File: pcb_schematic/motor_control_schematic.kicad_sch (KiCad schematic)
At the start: 1 part

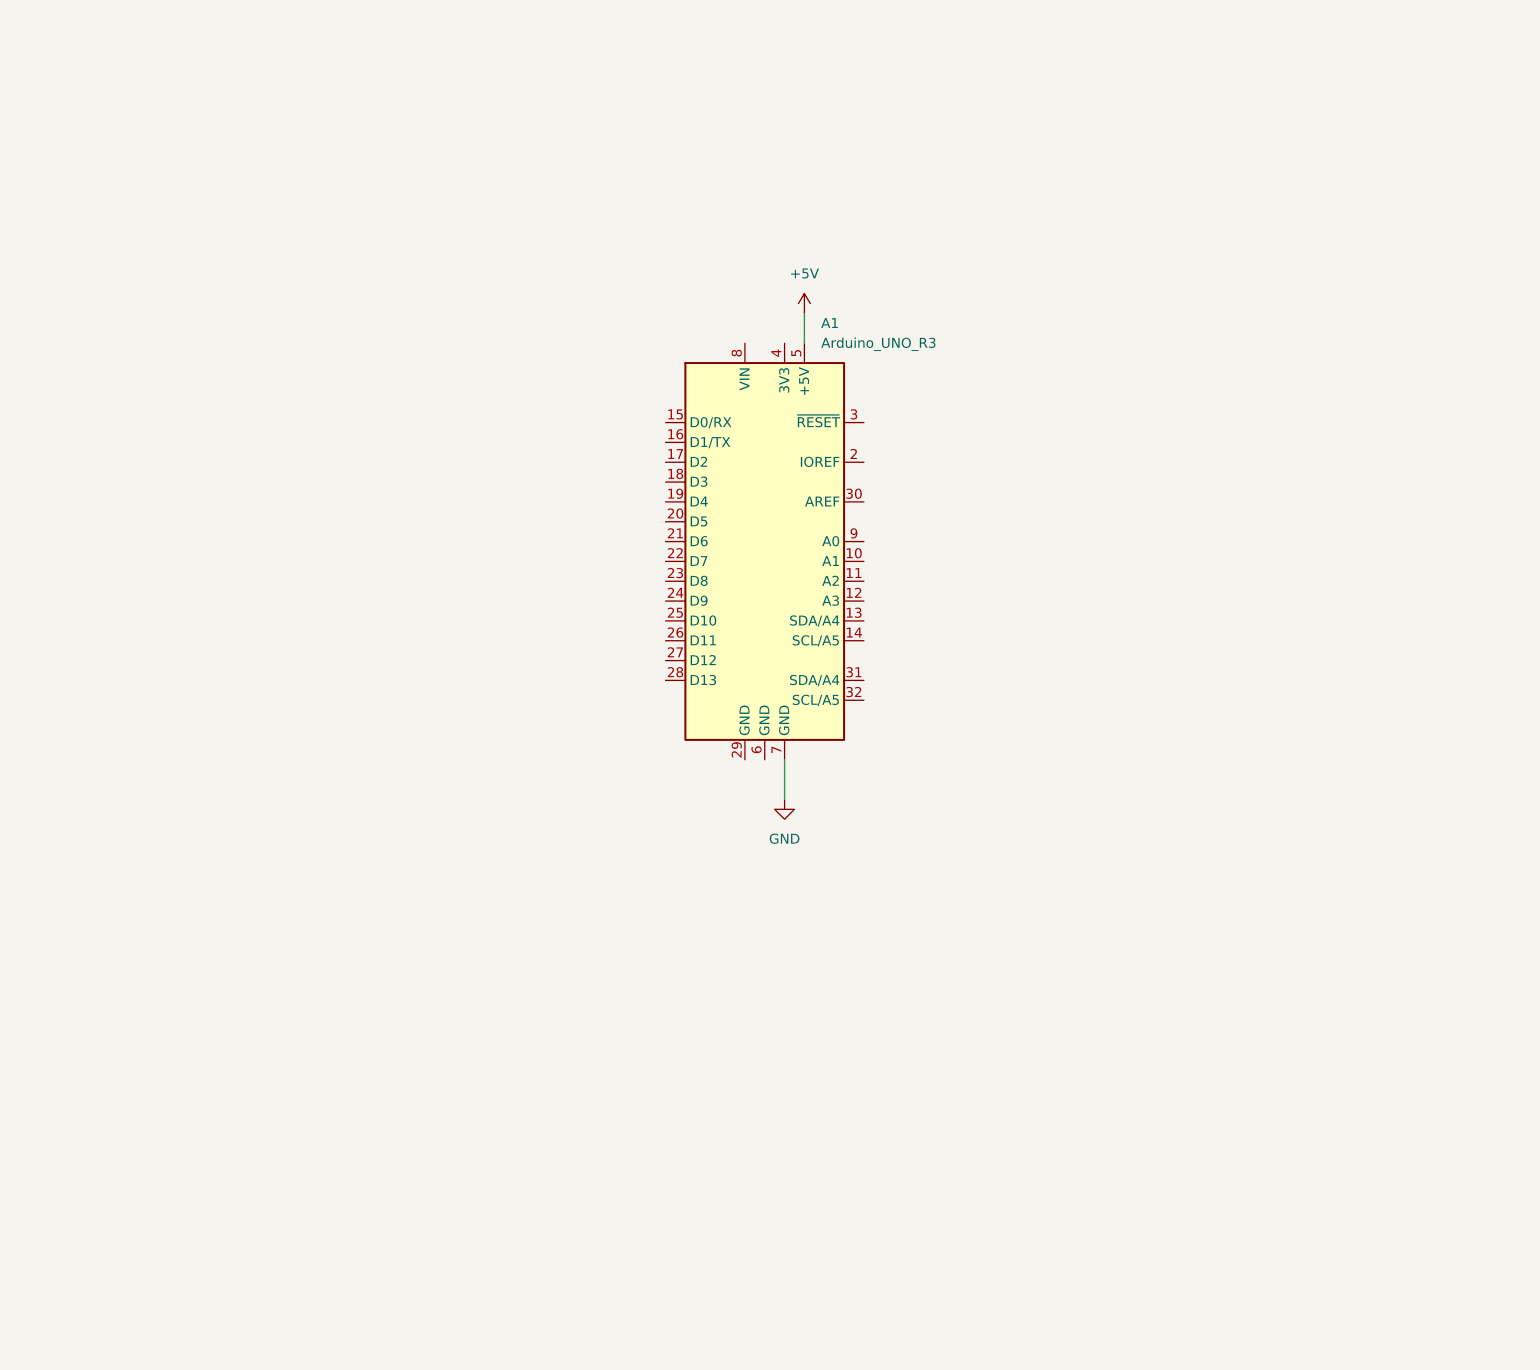
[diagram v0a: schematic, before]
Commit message: Finished arduino motor controller schematic
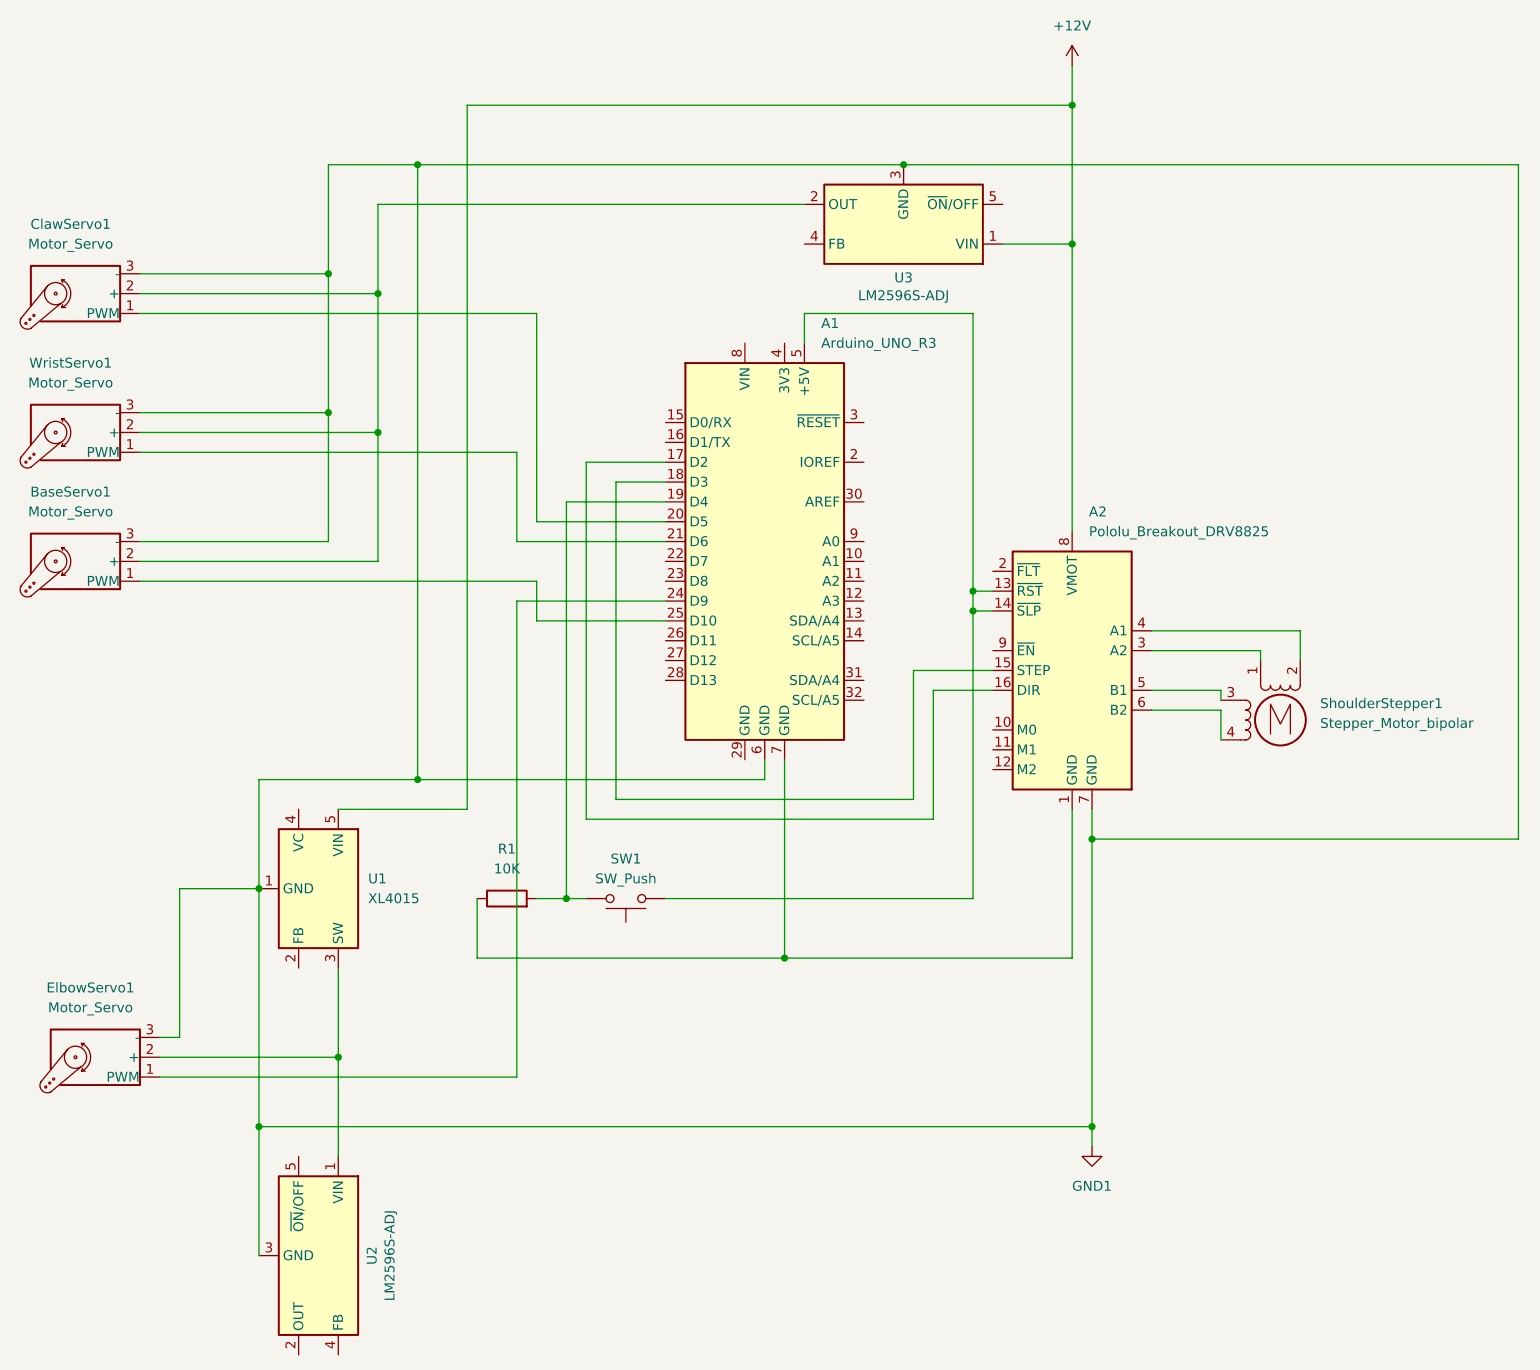
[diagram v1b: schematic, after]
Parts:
- added A2: Pololu_Breakout_DRV8825, Module:Pololu_Breakout-16_15.2x20.3mm, symbol Driver_Motor:Pololu_Breakout_DRV8825
- added BaseServo1, ClawServo1, ElbowServo1, WristServo1: Motor_Servo, Motors:Vybronics_VZ30C1T8219732L, symbol Motor:Motor_Servo
- added R1: 10K, Resistor_THT:R_Axial_DIN0204_L3.6mm_D1.6mm_P7.62mm_Horizontal, symbol Device:R
- added SW1: SW_Push, Button_Switch_THT:SW_XKB_DM1-16UP-1, symbol Switch:SW_Push
- added ShoulderStepper1: Stepper_Motor_bipolar, Motors:Vybronics_VZ30C1T8219732L, symbol Motor:Stepper_Motor_bipolar
- added U1: XL4015, Package_TO_SOT_SMD:TO-263-5_TabPin3, symbol Regulator_Switching:XL4015
- added U2, U3: LM2596S-ADJ, Package_TO_SOT_SMD:TO-263-5_TabPin3, symbol Regulator_Switching:LM2596S-ADJ
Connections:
- net at A1.17 (D2): now also A2.16 (DIR)
- net at A1.18 (D3): now also A2.15 (STEP)
- net at A1.19 (D4): now also R1.2, SW1.2
- net at A1.20 (D5): now also ClawServo1.1 (PWM)
- net at A1.21 (D6): now also WristServo1.1 (PWM)
- net at A1.24 (D9): now also ElbowServo1.1 (PWM)
- net at A1.25 (D10): now also BaseServo1.1 (PWM)
- net GND1: now reaches A1.6 (GND)
- net GND1: now also A2.7 (GND), BaseServo1.3 (-), ClawServo1.3 (-), ElbowServo1.3 (-), U1.1 (GND), U2.3 (GND), U3.3 (GND), WristServo1.3 (-)
- net +5V: no longer names the net of A1.5 (+5V)
- net +5V: now also A2.13 (~{RST}), A2.14 (~{SLP}), SW1.1
- net GND: no longer names the net of A1.7 (GND)
- net GND: now also A2.1 (GND), R1.1
- new net: A2.3 (A2), ShoulderStepper1.1
- new net: A2.4 (A1), ShoulderStepper1.2 (-)
- new net: A2.5 (B1), ShoulderStepper1.3
- new net: A2.6 (B2), ShoulderStepper1.4
- new net: ElbowServo1.2 (+), U1.3 (SW), U2.1 (VIN)
- new net: BaseServo1.2 (+), ClawServo1.2 (+), U3.2 (OUT), WristServo1.2 (+)
- new net +12V: A2.8 (VMOT), U1.5 (VIN), U3.1 (VIN)
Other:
- title: (none) -> Arduino Motor Controller
